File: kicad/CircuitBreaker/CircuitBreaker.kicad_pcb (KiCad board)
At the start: 2 copper layers, 71.6 x 30 mm, 4 parts

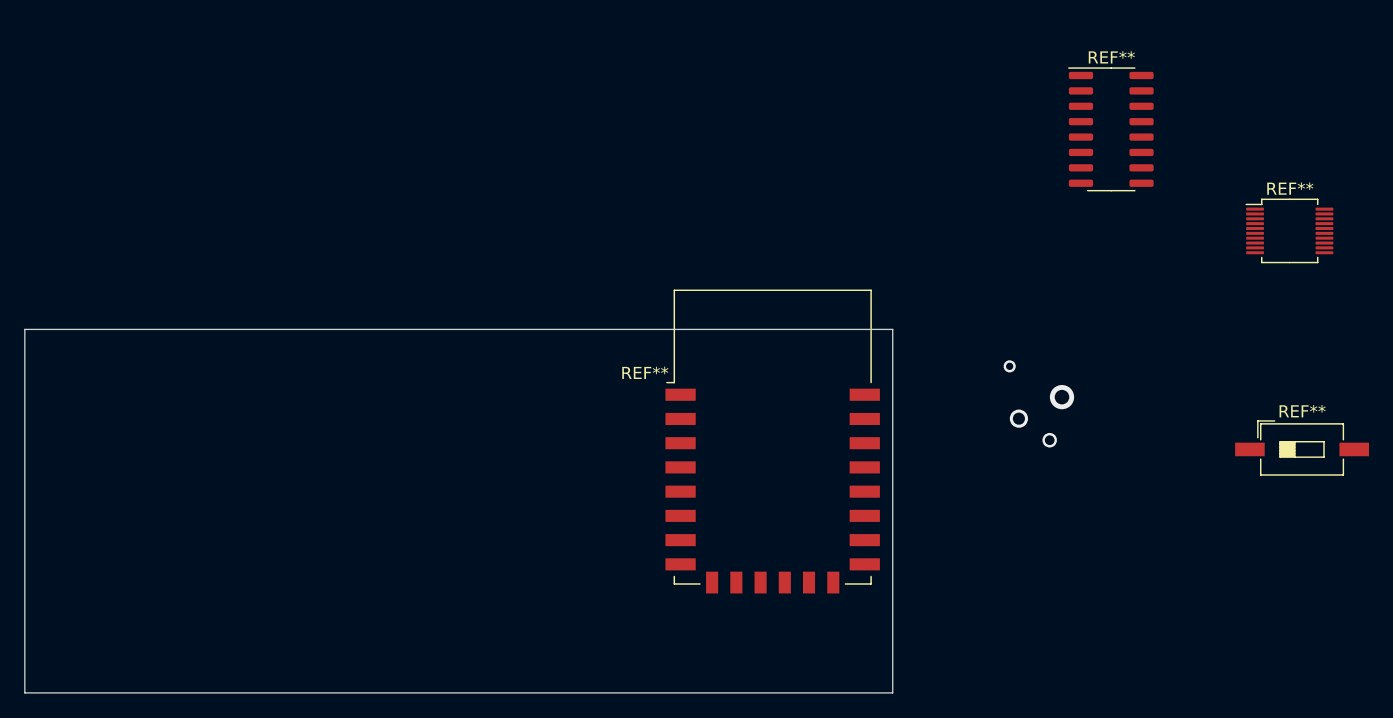
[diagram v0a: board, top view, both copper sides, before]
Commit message: circuit breaker pcb layout
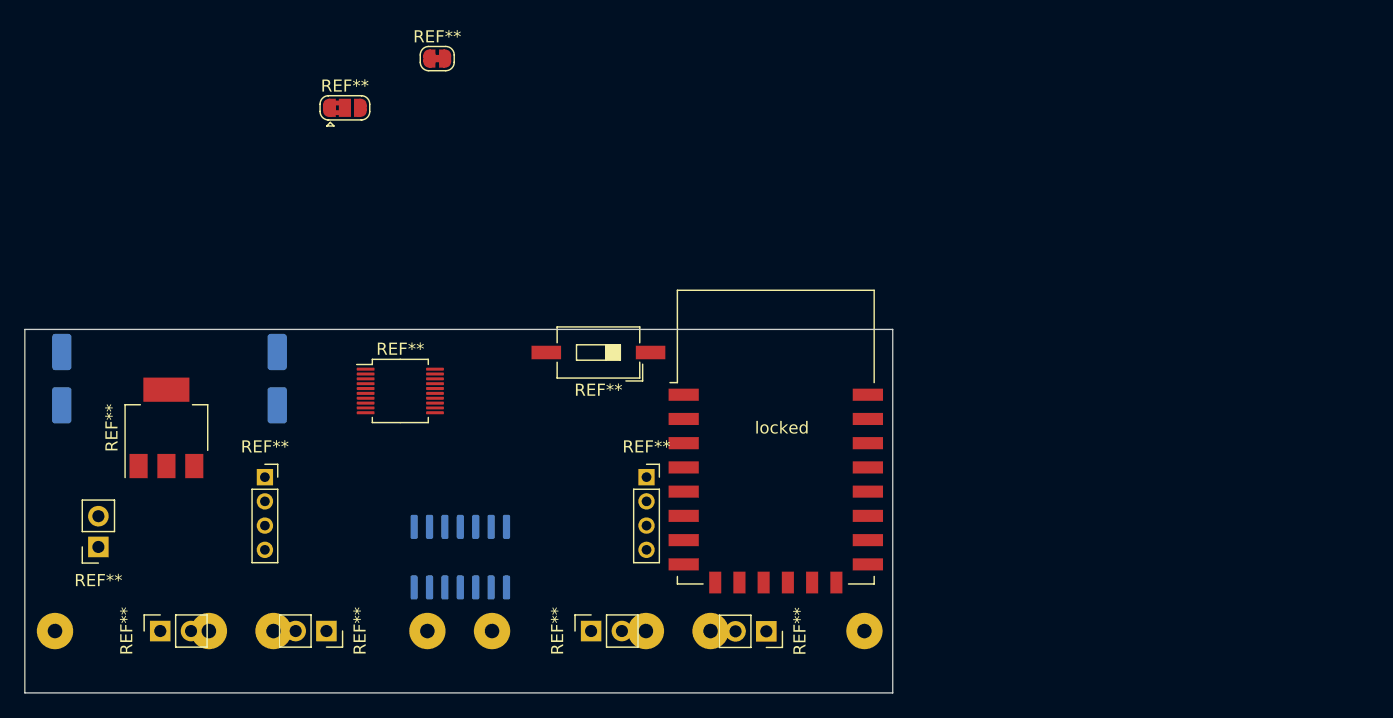
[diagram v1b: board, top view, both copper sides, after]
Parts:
- removed the REF** at (140.5, 34.3)
- added REF**: PinSocket_1x02_P2.54mm_Vertical, Connector_PinSocket_2.54mm:PinSocket_1x02_P2.54mm_Vertical, F.Cu at (56.9, 68.8)
- added REF**: PinSocket_1x02_P2.54mm_Vertical, Connector_PinSocket_2.54mm:PinSocket_1x02_P2.54mm_Vertical, F.Cu at (75.7, 75.7)
- added REF**: PinSocket_1x02_P2.54mm_Vertical, Connector_PinSocket_2.54mm:PinSocket_1x02_P2.54mm_Vertical, F.Cu at (112.0, 75.7)
- added REF**: CP_Elec_5x3, Capacitor_SMD:CP_Elec_5x3, B.Cu at (53.8, 54.9)
- added REF**: CP_Elec_5x3, Capacitor_SMD:CP_Elec_5x3, B.Cu at (71.6, 54.9)
- added REF**: Transformer_CT204D, lib:Transformer_CT204D, B.Cu at (113.7, 75.7)
- added REF**: locked, lib:SOP-14_3.9x9.9mm_P1.27mm, B.Cu at (87.4, 69.6)
- added REF**: Transformer_CT204D, lib:Transformer_CT204D, B.Cu at (59.6, 75.7)
- added REF**: PinSocket_1x04_P2.00mm_Vertical, Connector_PinSocket_2.00mm:PinSocket_1x04_P2.00mm_Vertical, F.Cu at (70.6, 63.0)
- added REF**: PinSocket_1x02_P2.54mm_Vertical, Connector_PinSocket_2.54mm:PinSocket_1x02_P2.54mm_Vertical, F.Cu at (97.5, 75.7)
- added REF**: PinSocket_1x02_P2.54mm_Vertical, Connector_PinSocket_2.54mm:PinSocket_1x02_P2.54mm_Vertical, F.Cu at (62.0, 75.7)
- added REF**: PinSocket_1x04_P2.00mm_Vertical, Connector_PinSocket_2.00mm:PinSocket_1x04_P2.00mm_Vertical, F.Cu at (102.1, 63.0)
- added REF**: SolderJumper-2_P1.3mm_Bridged_RoundedPad1.0x1.5mm, Jumper:SolderJumper-2_P1.3mm_Bridged_RoundedPad1.0x1.5mm, F.Cu at (84.8, 28.4)
- added REF**: SOT-223, Package_TO_SOT_SMD:SOT-223, F.Cu at (62.5, 58.9)
- added REF**: SolderJumper-3_P1.3mm_Bridged2Bar12_RoundedPad1.0x1.5mm, Jumper:SolderJumper-3_P1.3mm_Bridged2Bar12_RoundedPad1.0x1.5mm, F.Cu at (77.2, 32.5)
- added locked: locked, lib:Transformer_CT204D, B.Cu at (77.7, 75.7)
- added locked: locked, lib:Transformer_CT204D, B.Cu at (95.7, 75.7)
- moved REF** 74.6 mm to (81.8, 55.9)
- moved REF** 58.6 mm to (98.1, 52.7), turned to 180 degrees
- moved locked 0.25 mm to (112.8, 59.7)
- renumbered REF** to locked
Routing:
- net (no net): vias 4 -> 0

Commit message: ccb pcb rev
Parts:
- removed the REF** at (75.7, 75.7)
- removed the REF** at (97.5, 75.7)
- added REF**: R_Axial_DIN0204_L3.6mm_D1.6mm_P1.90mm_Vertical, Resistor_THT:R_Axial_DIN0204_L3.6mm_D1.6mm_P1.90mm_Vertical, F.Cu at (97.0, 62.9)
- added REF**: R_Axial_DIN0204_L3.6mm_D1.6mm_P1.90mm_Vertical, Resistor_THT:R_Axial_DIN0204_L3.6mm_D1.6mm_P1.90mm_Vertical, F.Cu at (93.0, 62.9)
- added REF**: R_Axial_DIN0204_L3.6mm_D1.6mm_P1.90mm_Vertical, Resistor_THT:R_Axial_DIN0204_L3.6mm_D1.6mm_P1.90mm_Vertical, F.Cu at (79.2, 66.0)
- added REF**: R_Axial_DIN0204_L3.6mm_D1.6mm_P1.90mm_Vertical, Resistor_THT:R_Axial_DIN0204_L3.6mm_D1.6mm_P1.90mm_Vertical, F.Cu at (75.2, 66.0)
- REF**: moved to F.Cu
- REF** (x2): moved to B.Cu
- moved REF** 52.3 mm to (114.3, 66.0), turned to -90 degrees
- moved REF** 46.4 mm to (117.9, 58.9), turned to 0 degrees
- moved REF** 26.6 mm to (71.6, 54.5)
- moved REF** 14.7 mm to (53.3, 69.6), turned to -90 degrees
- moved REF** 6.31 mm to (66.1, 70.9), turned to 0 degrees
- moved REF** 4.57 mm to (107.7, 74.2), turned to -135 degrees
- moved REF** 3.77 mm to (57.4, 65.0), turned to 0 degrees
- moved REF** 2.03 mm to (83.8, 55.9)
- moved REF** 1.83 mm to (101.1, 61.5)
- moved REF** 1.52 mm to (70.6, 61.5)
- moved REF** 1.12 mm to (86.9, 68.6), turned to 0 degrees

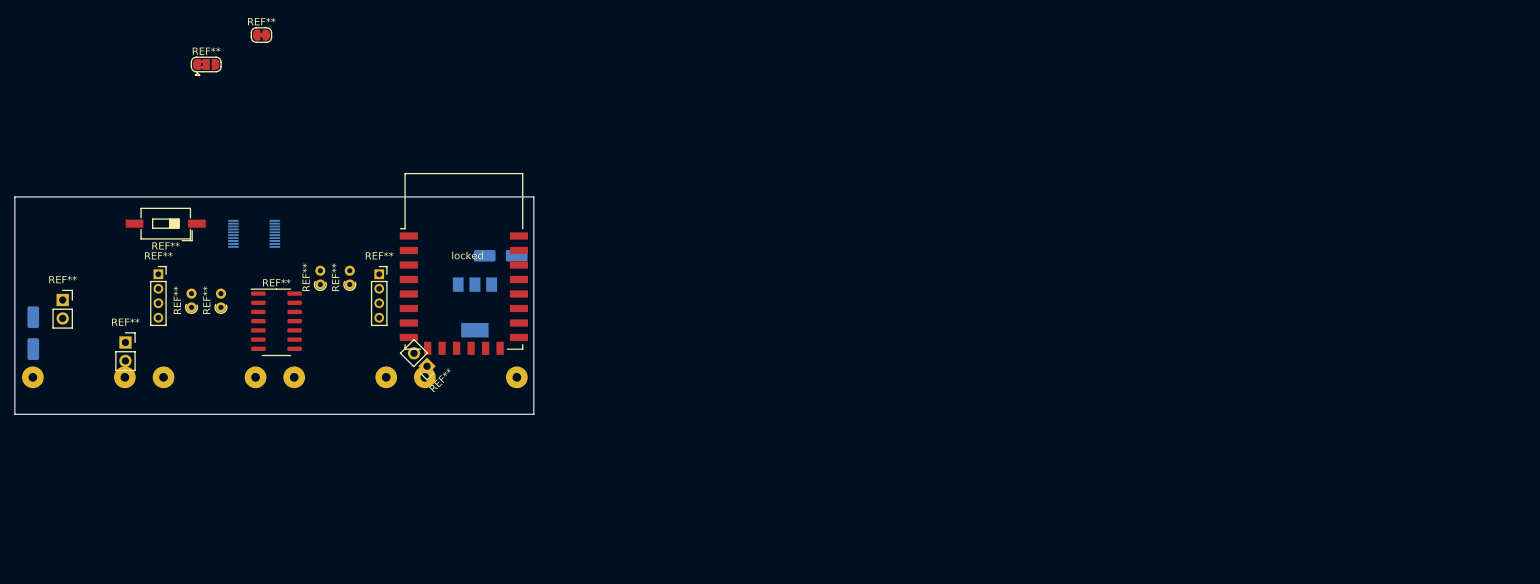
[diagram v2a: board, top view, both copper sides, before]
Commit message: net mapped to pcb
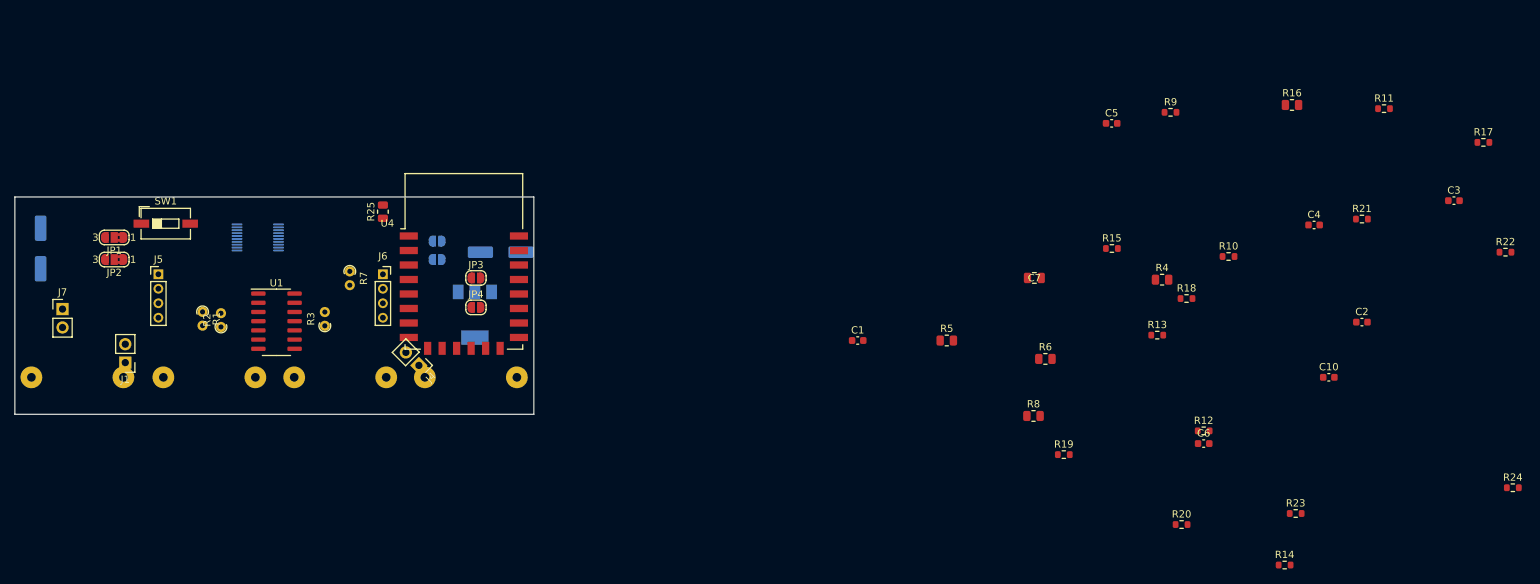
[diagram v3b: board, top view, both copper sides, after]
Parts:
- removed REF** (x3): PinSocket_1x02_P2.54mm_Vertical, Connector_PinSocket_2.54mm:PinSocket_1x02_P2.54mm_Vertical
- removed REF**: SW_DIP_SPSTx01_Slide_6.7x4.1mm_W8.61mm_P2.54mm_LowProfile, Button_Switch_SMD:SW_DIP_SPSTx01_Slide_6.7x4.1mm_W8.61mm_P2.54mm_LowProfile
- removed REF**: locked, lib:SOP-14_3.9x9.9mm_P1.27mm
- removed REF** (x4): R_Axial_DIN0204_L3.6mm_D1.6mm_P1.90mm_Vertical, Resistor_THT:R_Axial_DIN0204_L3.6mm_D1.6mm_P1.90mm_Vertical
- removed REF** (x2): CP_Elec_5x3, Capacitor_SMD:CP_Elec_5x3
- removed REF** (x2): Transformer_CT204D, lib:Transformer_CT204D
- removed REF**: SOT-223, Package_TO_SOT_SMD:SOT-223
- removed REF**: TSSOP-20_4.4x5mm_P0.4mm, Package_SO:TSSOP-20_4.4x5mm_P0.4mm
- removed REF** (x2): PinSocket_1x04_P2.00mm_Vertical, Connector_PinSocket_2.00mm:PinSocket_1x04_P2.00mm_Vertical
- removed REF**: SolderJumper-2_P1.3mm_Bridged_RoundedPad1.0x1.5mm, Jumper:SolderJumper-2_P1.3mm_Bridged_RoundedPad1.0x1.5mm
- removed REF**: SolderJumper-3_P1.3mm_Bridged2Bar12_RoundedPad1.0x1.5mm, Jumper:SolderJumper-3_P1.3mm_Bridged2Bar12_RoundedPad1.0x1.5mm
- removed locked: ESP-12E, RF_Module:ESP-12E
- removed locked (x2): locked, lib:Transformer_CT204D
- added C1: 1uF, Capacitor_SMD:C_0603_1608Metric, F.Cu at (167.1, 70.6)
- added C10: 0.1uF, Capacitor_SMD:C_0603_1608Metric, F.Cu at (232.2, 75.7)
- added C2: 1uF, Capacitor_SMD:C_0603_1608Metric, F.Cu at (236.7, 68.1)
- added C3: 1uF, Capacitor_SMD:C_0603_1608Metric, F.Cu at (249.4, 51.3)
- added C4: 1uF, Capacitor_SMD:C_0603_1608Metric, F.Cu at (230.1, 54.7)
- added C5: 0.1uF, Capacitor_SMD:C_0603_1608Metric, F.Cu at (202.2, 40.6)
- added C6: 0.1uF, Capacitor_SMD:C_0603_1608Metric, F.Cu at (214.9, 84.8)
- added C7: 22uF, Capacitor_SMD:C_0805_2012Metric, F.Cu at (191.5, 62.0)
- added C8: 220uF, Capacitor_SMD:CP_Elec_6.3x5.2, B.Cu at (54.4, 57.9)
- added C9: 100uF, Capacitor_SMD:CP_Elec_6.3x5.2, B.Cu at (117.9, 58.4)
- added J1: PH2.54, Connector_PinHeader_2.54mm:PinHeader_1x02_P2.54mm_Vertical, F.Cu at (66.0, 73.7)
- added J4: PH2.54, Connector_PinHeader_2.54mm:PinHeader_1x02_P2.54mm_Vertical, F.Cu at (106.6, 74.1)
- added J5: Conn_01x04_downlink, Connector_PinHeader_2.00mm:PinHeader_1x04_P2.00mm_Vertical, F.Cu at (70.6, 61.5)
- added J6: Conn_01x04_uplink, Connector_PinSocket_2.00mm:PinSocket_1x04_P2.00mm_Vertical, F.Cu at (101.6, 61.5)
- added J7: PH2.54, Connector_PinHeader_2.54mm:PinHeader_1x02_P2.54mm_Vertical, F.Cu at (57.4, 66.3)
- added JP1: bus-type, Jumper:SolderJumper-3_P1.3mm_Bridged2Bar12_RoundedPad1.0x1.5mm_NumberLabels, F.Cu at (64.5, 56.4)
- added JP2: bus-type, Jumper:SolderJumper-3_P1.3mm_Bridged2Bar12_RoundedPad1.0x1.5mm_NumberLabels, F.Cu at (64.5, 59.4)
- added JP3: I2C, Jumper:SolderJumper-2_P1.3mm_Open_RoundedPad1.0x1.5mm, F.Cu at (114.4, 62.0)
- added JP4: I2C, Jumper:SolderJumper-2_P1.3mm_Open_RoundedPad1.0x1.5mm, F.Cu at (114.4, 66.0)
- added JP5: dbg-sel, Jumper:SolderJumper-2_P1.3mm_Open_RoundedPad1.0x1.5mm, B.Cu at (109.1, 56.9)
- added JP6: dbg-sel, Jumper:SolderJumper-2_P1.3mm_Open_RoundedPad1.0x1.5mm, B.Cu at (109.1, 59.4)
- added R1: 120, Resistor_THT:R_Axial_DIN0204_L3.6mm_D1.6mm_P1.90mm_Vertical, F.Cu at (76.7, 66.7)
- added R10: 47K, Resistor_SMD:R_0603_1608Metric, F.Cu at (218.3, 59.0)
- added R11: 47K, Resistor_SMD:R_0603_1608Metric, F.Cu at (239.8, 38.6)
- added R12: 47K, Resistor_SMD:R_0603_1608Metric, F.Cu at (214.9, 83.1)
- added R13: 10K, Resistor_SMD:R_0603_1608Metric, F.Cu at (208.5, 69.9)
- added R14: 10K, Resistor_SMD:R_0603_1608Metric, F.Cu at (226.1, 101.6)
- added R15: 10K, Resistor_SMD:R_0603_1608Metric, F.Cu at (202.2, 57.9)
- added R16: 300, Resistor_SMD:R_0805_2012Metric, F.Cu at (227.1, 38.1)
- added R17: 10K, Resistor_SMD:R_0603_1608Metric, F.Cu at (253.5, 43.3)
- added R18: 22, Resistor_SMD:R_0603_1608Metric, F.Cu at (212.5, 64.8)
- added R19: 22, Resistor_SMD:R_0603_1608Metric, F.Cu at (195.6, 86.4)
- added R2: 120, Resistor_THT:R_Axial_DIN0204_L3.6mm_D1.6mm_P1.90mm_Vertical, F.Cu at (79.2, 68.7)
- added R20: 10K, Resistor_SMD:R_0603_1608Metric, F.Cu at (211.8, 96.0)
- added R21: 10K, Resistor_SMD:R_0603_1608Metric, F.Cu at (236.7, 53.8)
- added R22: 10K, Resistor_SMD:R_0603_1608Metric, F.Cu at (256.5, 58.4)
- added R23: 10K, Resistor_SMD:R_0603_1608Metric, F.Cu at (227.6, 94.5)
- added R24: 10K, Resistor_SMD:R_0603_1608Metric, F.Cu at (257.6, 90.9)
- added R25: 1M, Resistor_SMD:R_0805_2012Metric, F.Cu at (101.6, 52.8)
- added R3: 120, Resistor_THT:R_Axial_DIN0204_L3.6mm_D1.6mm_P1.90mm_Vertical, F.Cu at (93.6, 68.6)
- added R4: 240, Resistor_SMD:R_0805_2012Metric, F.Cu at (209.1, 62.2)
- added R5: 240, Resistor_SMD:R_0805_2012Metric, F.Cu at (179.4, 70.6)
- added R6: 240, Resistor_SMD:R_0805_2012Metric, F.Cu at (193.0, 73.2)
- added R7: 120, Resistor_THT:R_Axial_DIN0204_L3.6mm_D1.6mm_P1.90mm_Vertical, F.Cu at (97.0, 61.1)
- added R8: 240, Resistor_SMD:R_0805_2012Metric, F.Cu at (191.4, 81.0)
- added R9: 47K, Resistor_SMD:R_0603_1608Metric, F.Cu at (210.3, 39.1)
- added SW1: usbIAP, Button_Switch_SMD:SW_DIP_SPSTx01_Slide_6.7x4.1mm_W6.73mm_P2.54mm_LowProfile_JPin, F.Cu at (71.6, 54.5)
- added T1: CT104D, lib:Transformer_CT204D, B.Cu at (59.4, 75.7)
- added T2: CT104D, lib:Transformer_CT204D, B.Cu at (77.6, 75.7)
- added T3: CT104D, lib:Transformer_CT204D, B.Cu at (95.7, 75.7)
- added T4: CT104D, lib:Transformer_CT204D, B.Cu at (113.7, 75.7)
- added U1: LM324, lib:SOP-14_3.9x9.9mm_P1.27mm, F.Cu at (86.9, 68.6)
- added U2: STC8H8K64U-45I-TSSOP20, Package_SO:TSSOP-20_4.4x5mm_P0.4mm, B.Cu at (84.3, 56.4)
- added U3: AP1117-33, Package_TO_SOT_SMD:SOT-223-3_TabPin2, B.Cu at (114.3, 67.1)
- added U4: ESP-12E, RF_Module:ESP-12E, F.Cu at (112.8, 59.7)

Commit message: pcb rev
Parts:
- added D1: green, LED_SMD:LED_0603_1608Metric, F.Cu at (99.1, 55.7)
- added D2: blue, LED_SMD:LED_0603_1608Metric, F.Cu at (97.3, 55.7)
- added R26: 4K7, Resistor_SMD:R_0603_1608Metric, B.Cu at (99.1, 55.7)
- added R27: 4K7, Resistor_SMD:R_0603_1608Metric, B.Cu at (97.3, 55.7)
- C1, C10, C2, C3, C4, C5, C6, C7, R10, R11, R12, R15, R16, R17, R18, R19, R20, R21, R22, R23, R24, R4, R5, R6, R8, R9: moved to B.Cu
- JP5, JP6: footprint Jumper:SolderJumper-2_P1.3mm_Open_RoundedPad1.0x1.5mm -> Jumper:SolderJumper-2_P1.3mm_Bridged_RoundedPad1.0x1.5mm
- R1, R2, R3, R7: footprint Resistor_THT:R_Axial_DIN0204_L3.6mm_D1.6mm_P1.90mm_Vertical -> Resistor_THT:R_Axial_DIN0204_L3.6mm_D1.6mm_P7.62mm_Horizontal
- U2: value STC8H8K64U-45I-TSSOP20 -> STC8H8K64U
- moved R16 161.4 mm to (66.7, 56.0), turned to -90 degrees
- moved C2 157.3 mm to (79.5, 64.0)
- moved C3 156.6 mm to (93.3, 63.8), turned to 180 degrees
- moved R14 154.9 mm to (74.4, 69.8), turned to 90 degrees
- moved R24 153.1 mm to (106.4, 66.5), turned to -90 degrees
- moved R11 148.4 mm to (93.3, 62.2), turned to 180 degrees
- moved R10 138.9 mm to (79.5, 62.5)
- moved C6 138.2 mm to (79.8, 55.6), turned to 90 degrees
- moved R9 136.6 mm to (76.0, 64.0), turned to 180 degrees
- moved R22 136.3 mm to (120.4, 65.2), turned to -90 degrees
- moved R13 135.6 mm to (72.9, 69.8), turned to 90 degrees
- moved R17 135.1 mm to (120.9, 69.4), turned to 90 degrees
- moved R15 133.8 mm to (68.5, 55.9), turned to 90 degrees
- moved C4 133.6 mm to (96.8, 63.8)
- moved R4 132.5 mm to (76.7, 66.5), turned to -90 degrees
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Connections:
- U2 pad 17: unconnected-(U2-Pad17) -> Net-(U2-Pad17)
- U2 pad 18: unconnected-(U2-Pad18) -> Net-(U2-Pad18)
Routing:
- added copper zone on B.Cu, net GND
- added copper zone on F.Cu, net GND
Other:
- board size 71.6 x 30 mm -> 71.6 x 27.5 mm

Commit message: pcb all connected
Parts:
- R25: value 1M -> 5vUP
- U2: value STC8H8K64U -> STC8H8K64U-45I-TSSOP20
- turned C5 to -90 degrees
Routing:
- net GND: track 0.00 -> 221.2 mm, vias 0 -> 19
- net +5V: track 0.00 -> 122.4 mm, vias 0 -> 10
- net +3V3: track 0.00 -> 75.0 mm, vias 0 -> 3
- net DTXD: track 0.00 -> 36.6 mm, vias 0 -> 3
- net SDA: track 0.00 -> 35.8 mm, vias 0 -> 2
- net /RXD_UP: track 0.00 -> 33.2 mm, vias 0 -> 4
- net SCL: track 0.00 -> 33.1 mm, vias 0 -> 4
- net Net-(J1-Pad1): track 0.00 -> 31.8 mm
- net Net-(J4-Pad1): track 0.00 -> 30.1 mm, vias 0 -> 1
- net /TXD_UP: track 0.00 -> 28.5 mm, vias 0 -> 3
- net DRXD: track 0.00 -> 25.4 mm, vias 0 -> 3
- net Net-(R2-Pad2): track 0.00 -> 22.3 mm, vias 0 -> 1
- net ADC1: track 0.00 -> 22.3 mm, vias 0 -> 1
- net Net-(R15-Pad2): track 0.00 -> 22.3 mm, vias 0 -> 2
- net ADC2: track 0.00 -> 20.9 mm, vias 0 -> 2
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
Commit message: pcb err check
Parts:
- J5: value Conn_01x04_downlink -> downlink
- J6: value Conn_01x04_uplink -> uplink
- J7: value PH2.54 -> 5v
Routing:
- net GND: track 221.2 -> 216.4 mm, vias 19 -> 18
- net Net-(R2-Pad2): track 22.3 -> 17.7 mm
- net +5V: track 122.4 -> 119.9 mm
- net Net-(J4-Pad1): track 30.1 -> 31.6 mm
- net SDA: track 35.8 -> 34.4 mm
- net DRXD: track 25.4 -> 24.2 mm
- net +3V3: track 75.0 -> 74.3 mm
- net ADC2: track 20.9 -> 21.4 mm
